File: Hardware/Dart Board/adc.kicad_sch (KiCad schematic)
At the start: 2 parts, among them U1 ADS1115IDGS

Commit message: Piezo circuit
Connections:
- net PIEZO_01: now reaches U1.4 (AIN0)
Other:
- note removed: "piezo sensors here w/ protection"
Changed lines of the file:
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@@
 		(rev "01")
-	)
-	(text "piezo sensors here w/ protection"
-		(exclude_from_sim no)
-		(at 103.886 97.282 0)
-		(effects
-			(font
-				(size 1.27 1.27)
-			)
-		)
 	)
 	(junction
@@
 	(wire
 		(pts
+			(xy 104.14 93.98) (xy 121.92 93.98)
+		)
+		(stroke
+			(width 0)
+			(type default)
+		)
+	)
+	(wire
+		(pts
 			(xy 153.67 69.85) (xy 153.67 76.2)
 		)
@@
 				(hide yes)
 			)
+		)
+	)
+	(global_label "PIEZO_01"
+		(shape input)
+		(at 104.14 93.98 180)
+		(fields_autoplaced yes)
+		(effects
+			(font
+				(size 1.27 1.27)
+			)
+			(justify right)
+		)
+		(property "Intersheetrefs" "${INTERSHEET_REFS}"
+			(at 92.2044 93.98 0)
+			(effects
+				(font
+					(size 1.27 1.27)
+				)
+				(justify right)
+				(hide yes)
+			)

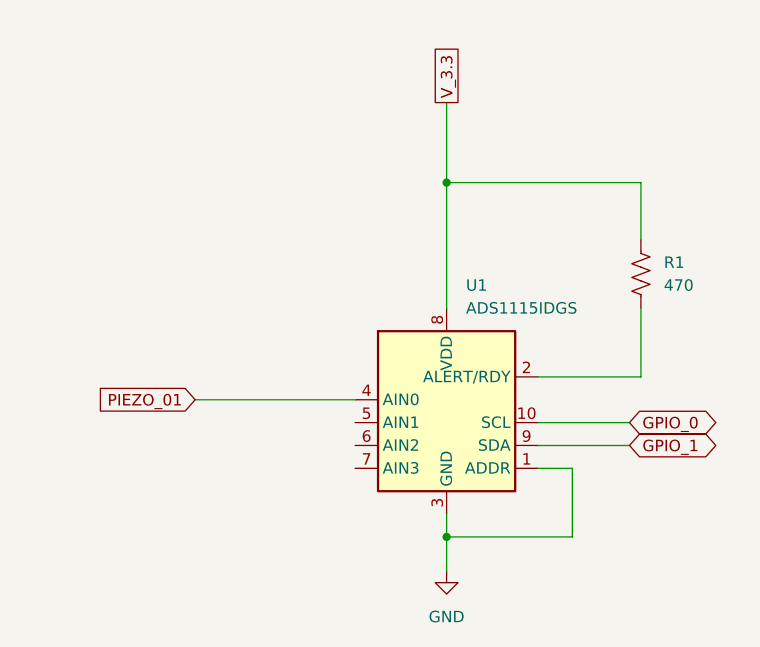
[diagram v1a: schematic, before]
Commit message: Assigned Footprints and added to PCB editor
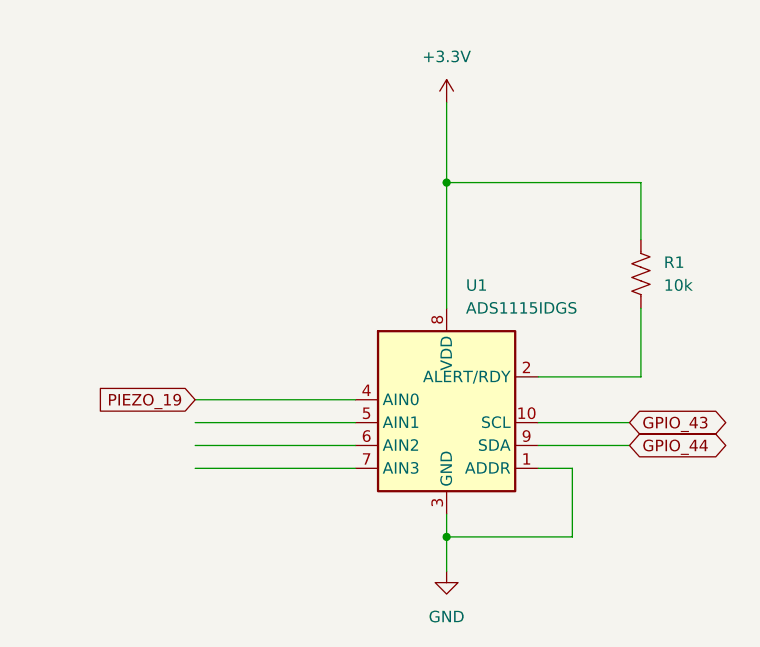
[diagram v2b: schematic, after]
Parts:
- R1: value 470 -> 10k; footprint (none) -> Resistor_SMD:R_0603_1608Metric_Pad0.98x0.95mm_HandSolder
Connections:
- net GPIO_0 renamed GPIO_43
- net GPIO_1 renamed GPIO_44
- net PIEZO_01 renamed PIEZO_19
- net V_3.3 renamed +3.3V
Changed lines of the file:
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@@
+	(wire
+		(pts
+			(xy 104.14 99.06) (xy 121.92 99.06)
+		)
+		(stroke
+			(width 0)
+			(type default)
+		)
+	)
 	(wire
 		(pts
@@
 	(wire
 		(pts
+			(xy 104.14 96.52) (xy 121.92 96.52)
+		)
+		(stroke
+			(width 0)
+			(type default)
+		)
+	)
+	(wire
+		(pts
+			(xy 104.14 101.6) (xy 121.92 101.6)
+		)
+		(stroke
+			(width 0)
+			(type default)
+		)
+	)
+	(wire
+		(pts
 			(xy 132.08 106.68) (xy 132.08 109.22)
 		)
@@
 		)
 	)
-	(global_label "GPIO_1"
+	(global_label "GPIO_44"
 		(shape bidirectional)
 		(at 152.4 99.06 0)
@@
 		)
 	)
-	(global_label "GPIO_0"
+	(global_label "GPIO_43"
 		(shape bidirectional)
 		(at 152.4 96.52 0)
@@
 		)
 		(property "Intersheetrefs" "${INTERSHEET_REFS}"
-			(at 163.1489 96.52 0)
+			(at 164.3584 96.52 0)
 			(effects
 				(font
@@
 		)
 	)
-	(global_label "V_3.3"
-		(shape passive)
-		(at 132.08 60.96 90)
-		(fields_autoplaced yes)
-		(effects
-			(font
-				(size 1.27 1.27)
-			)
-			(justify left)
-		)
-		(property "Intersheetrefs" "${INTERSHEET_REFS}"
-			(at 132.08 54.0061 90)
-			(effects
-				(font
-					(size 1.27 1.27)
-				)
-				(justify left)
-				(hide yes)
-			)
-		)
-	)
-	(global_label "PIEZO_01"
+	(global_label "PIEZO_19"
 		(shape input)
 		(at 104.14 93.98 180)
@@
 	)
 	(symbol
+		(lib_id "power:+3.3V")
+		(at 132.08 60.96 0)
+		(unit 1)
+		(exclude_from_sim no)
+		(in_bom yes)
+		(on_board yes)
+		(dnp no)
+		(fields_autoplaced yes)
+		(property "Reference" "#PWR024"
+			(at 132.08 64.77 0)
+			(effects
+				(font
+					(size 1.27 1.27)
+				)
+				(hide yes)
+			)
+		)
+		(property "Value" "+3.3V"
+			(at 132.08 55.88 0)
+			(effects
+				(font
+					(size 1.27 1.27)
+				)
+			)
+		)
+		(property "Footprint" ""
+			(at 132.08 60.96 0)
+			(effects
+				(font
+					(size 1.27 1.27)
+				)
+				(hide yes)
+			)
+		)
+		(property "Datasheet" ""
+			(at 132.08 60.96 0)
+			(effects
+				(font
+					(size 1.27 1.27)
+				)
+				(hide yes)
+			)
+		)
+		(property "Description" "Power symbol creates a global label with name \"+3.3V\""
+			(at 132.08 60.96 0)
+			(effects
+				(font
+					(size 1.27 1.27)
+				)
+				(hide yes)
+			)
+		)
+		(pin "1"
+		)
+		(instances
+			(project ""
+				(path "/1d6d0dd6-dd3e-4fbe-b34b-7dc303157c7e/903efdef-076c-4652-98a8-7ce1d4f31a0f"
+					(reference "#PWR024")
+					(unit 1)
+				)
+			)
+		)
+	)
+	(symbol
 		(lib_id "Device:R_US")
 		(at 153.67 80.01 0)
@@
 			)
 		)
-		(property "Value" "470"
+		(property "Value" "10k"
 			(at 156.21 81.2799 0)
 			(effects
@@
 			)
 		)
-		(property "Footprint" ""
+		(property "Footprint" "Resistor_SMD:R_0603_1608Metric_Pad0.98x0.95mm_HandSolder"
 			(at 154.686 80.264 90)
 			(effects
